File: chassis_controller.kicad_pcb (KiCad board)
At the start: 2 copper layers, 100 x 75 mm, 151 parts, among them J1 Screw_Terminal_01x02, J10 Conn_01x04_Pin, J12 Conn_01x04_Pin, J13 Conn_01x04_Pin, J14 Conn_01x04_Pin, J15 Conn_01x04_Pin, J16 Conn_01x04_Pin, J17 Conn_01x04_Pin, J18 Conn_01x03_Pin, J19 Conn_01x03_Pin, J2 Conn_01x04_Pin, J20 Conn_01x03_Pin, J21 Conn_01x04_Pin, J22 Conn_01x03_Pin, J23 Conn_01x03_Pin, J24 Conn_01x03_Pin, J25 Conn_01x03_Pin, J26 Conn_01x06_Pin, J3 Screw_Terminal_01x02, J4 Conn_01x02_Pin, J5 Conn_01x03_Pin, J6 Conn_01x03_Pin, J7 Conn_01x04_Pin, J8 Conn_01x04_Pin, J9 Conn_01x04_Pin, Q1 NMOS, Q2 HSBA100P04, Q3 NMOS, Q4 HSBA100P04, U1 AP64500SP-13, U2 AMS1117-3.3, U3 DSHP04TSGER, U4 STM32F407VGT6TR, U5 PCA9685PW,118, U6 PCA9685PW,118, U7 MPU-6050, U8 SN65HVD230DR, X1 X32258MOB4SI

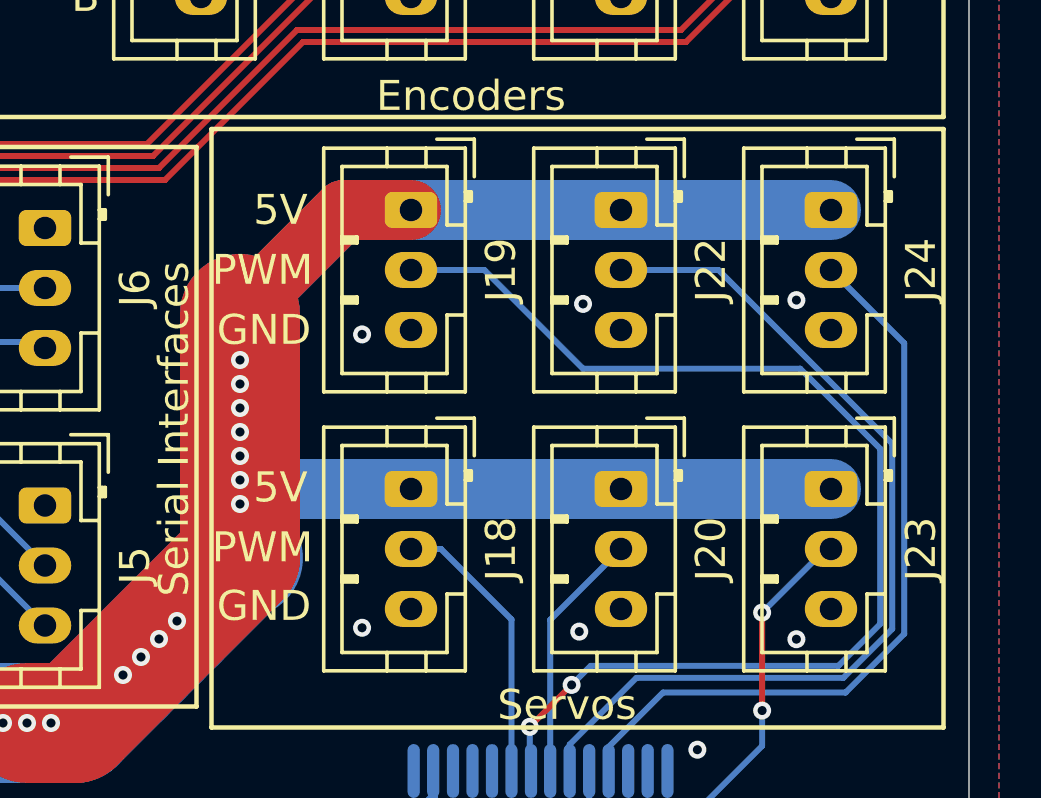
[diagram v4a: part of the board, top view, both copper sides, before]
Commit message: Fix servo power line
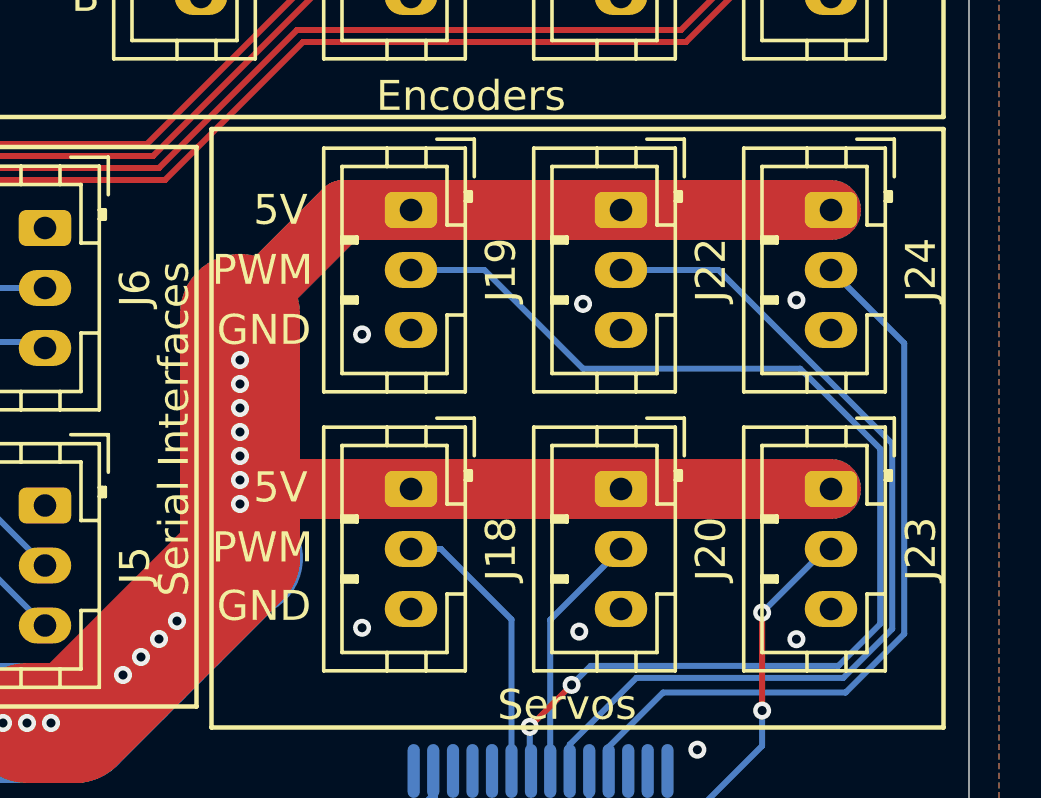
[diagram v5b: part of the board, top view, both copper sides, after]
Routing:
- net /SERVO_5V: track 95.4 -> 129.2 mm
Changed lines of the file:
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@@
+	)
+	(segment
+		(start 192.4 105.2)
+		(end 199.4 105.2)
+		(width 2)
+		(layer "F.Cu")
+		(net 63)
 	)
 	(segment
@@
 	)
 	(segment
+		(start 185.4 114.5)
+		(end 192.4 114.5)
+		(width 2)
+		(layer "F.Cu")
+		(net 63)
+	)
+	(segment
 		(start 179.7 110.2)
 		(end 179.7 108.663788)
@@
 	(segment
 		(start 179.7 116.786212)
-		(end 179.7 110.2)
-		(width 4)
+		(end 179.7 114.3)
+		(width 4)
+		(layer "F.Cu")
+		(net 63)
+	)
+	(segment
+		(start 185.4 105.2)
+		(end 192.4 105.2)
+		(width 2)
 		(layer "F.Cu")
 		(net 63)
@@
 	)
 	(segment
+		(start 192.4 114.5)
+		(end 199.4 114.5)
+		(width 2)
+		(layer "F.Cu")
+		(net 63)
+	)
+	(segment
+		(start 179.7 114.3)
+		(end 179.9 114.5)
+		(width 2)
+		(layer "F.Cu")
+		(net 63)
+	)
+	(segment
 		(start 174.186212 122.3)
 		(end 179.7 116.786212)
@@
 	)
 	(segment
+		(start 179.9 114.5)
+		(end 185.4 114.5)
+		(width 2)
+		(layer "F.Cu")
+		(net 63)
+	)
+	(segment
+		(start 179.7 114.3)
+		(end 179.7 110.2)
+		(width 4)
+		(layer "F.Cu")
+		(net 63)
+	)
+	(segment
 		(start 185.4 105.2)
 		(end 183.163788 105.2)
@@
 	)
 	(segment
+		(start 192.4 114.5)
+		(end 199.4 114.5)
+		(width 2)
+		(layer "B.Cu")
+		(net 63)
+	)
+	(segment
 		(start 179.7 111)
 		(end 179.7 110.2)
@@
 	)
 	(segment
+		(start 185.4 114.5)
+		(end 192.4 114.5)
+		(width 2)
+		(layer "B.Cu")
+		(net 63)
+	)
+	(segment
+		(start 180 114.5)
+		(end 179.7 114.2)
+		(width 2)
+		(layer "B.Cu")
+		(net 63)
+	)
+	(segment
+		(start 170.2 122.3)
+		(end 171 122.3)
+		(width 4)
+		(layer "B.Cu")
+		(net 63)
+	)
+	(segment
+		(start 171.8 122.3)
+		(end 172.6 122.3)
+		(width 4)
+		(layer "B.Cu")
+		(net 63)
+	)
+	(segment
+		(start 192.4 105.2)
+		(end 199.4 105.2)
+		(width 2)
+		(layer "B.Cu")
+		(net 63)
+	)
+	(segment
+		(start 177.6 118.9)
+		(end 179.7 116.8)
+		(width 4)
+		(layer "B.Cu")
+		(net 63)
+	)
+	(segment
+		(start 179.7 114.2)
+		(end 179.7 113.4)
+		(width 4)
+		(layer "B.Cu")
+		(net 63)
+	)
+	(segment
+		(start 179.7 116.8)
+		(end 179.7 115)
+		(width 4)
+		(layer "B.Cu")
+		(net 63)
+	)
+	(segment
+		(start 165.06 125.234336)
+		(end 167.994336 122.3)
+		(width 4)
+		(layer "B.Cu")
+		(net 63)
+	)
+	(segment
+		(start 167.994336 122.3)
+		(end 170.2 122.3)
+		(width 4)
+		(layer "B.Cu")
+		(net 63)
+	)
+	(segment
+		(start 179.7 116.8)
+		(end 179.8 116.8)
+		(width 4)
+		(layer "B.Cu")
+		(net 63)
+	)
+	(segment
+		(start 171 122.3)
+		(end 171.8 122.3)
+		(width 4)
+		(layer "B.Cu")
+		(net 63)
+	)
+	(segment
+		(start 176.4 120.1)
+		(end 177 119.5)
+		(width 4)
+		(layer "B.Cu")
+		(net 63)
+	)
+	(segment
+		(start 173.4 122.3)
+		(end 174.2 122.3)
+		(width 4)
+		(layer "B.Cu")
+		(net 63)
+	)
+	(segment
+		(start 165.06 128.645)
+		(end 165.06 125.234336)
+		(width 4)
+		(layer "B.Cu")
+		(net 63)
+	)
+	(segment
+		(start 179.7 111.8)
+		(end 179.7 111)
+		(width 4)
+		(layer "B.Cu")
+		(net 63)
+	)
+	(segment
+		(start 175.8 120.7)
+		(end 176.4 120.1)
+		(width 4)
+		(layer "B.Cu")
+		(net 63)
+	)
+	(segment
+		(start 179.7 110.2)
+		(end 179.7 108.663788)
+		(width 4)
+		(layer "B.Cu")
+		(net 63)
+	)
+	(segment
+		(start 179.7 108.663788)
+		(end 183.163788 105.2)
+		(width 2)
+		(layer "B.Cu")
+		(net 63)
+	)
+	(segment
 		(start 185.4 105.2)
 		(end 192.4 105.2)
 		(width 2)
 		(layer "B.Cu")
-		(net 63)
-	)
-	(segment
-		(start 180 114.5)
-		(end 179.7 114.2)
-		(width 2)
-		(layer "B.Cu")
-		(net 63)
-	)
-	(segment
-		(start 170.2 122.3)
-		(end 171 122.3)
-		(width 4)
-		(layer "B.Cu")
-		(net 63)
-	)
-	(segment
-		(start 171.8 122.3)
-		(end 172.6 122.3)
-		(width 4)
-		(layer "B.Cu")
-		(net 63)
-	)
-	(segment
-		(start 177.6 118.9)
-		(end 179.7 116.8)
-		(width 4)
-		(layer "B.Cu")
-		(net 63)
-	)
-	(segment
-		(start 199.4 114.5)
-		(end 192.4 114.5)
-		(width 2)
-		(layer "B.Cu")
-		(net 63)
-	)
-	(segment
-		(start 179.7 114.2)
-		(end 179.7 113.4)
-		(width 4)
-		(layer "B.Cu")
-		(net 63)
-	)
-	(segment
-		(start 192.4 105.2)
-		(end 199.4 105.2)
-		(width 2)
-		(layer "B.Cu")
-		(net 63)
-	)
-	(segment
-		(start 179.7 116.8)
-		(end 179.7 115)
-		(width 4)
-		(layer "B.Cu")
-		(net 63)
-	)
-	(segment
-		(start 165.06 125.234336)
-		(end 167.994336 122.3)
-		(width 4)
-		(layer "B.Cu")
-		(net 63)
-	)
-	(segment
-		(start 167.994336 122.3)
-		(end 170.2 122.3)
-		(width 4)
-		(layer "B.Cu")
-		(net 63)
-	)
-	(segment
-		(start 179.7 116.8)
-		(end 179.8 116.8)
-		(width 4)
-		(layer "B.Cu")
-		(net 63)
-	)
-	(segment
-		(start 171 122.3)
-		(end 171.8 122.3)
-		(width 4)
-		(layer "B.Cu")
-		(net 63)
-	)
-	(segment
-		(start 176.4 120.1)
-		(end 177 119.5)
-		(width 4)
-		(layer "B.Cu")
-		(net 63)
-	)
-	(segment
-		(start 173.4 122.3)
-		(end 174.2 122.3)
-		(width 4)
-		(layer "B.Cu")
-		(net 63)
-	)
-	(segment
-		(start 192.4 114.5)
-		(end 185.4 114.5)
-		(width 2)
-		(layer "B.Cu")
-		(net 63)
-	)
-	(segment
-		(start 165.06 128.645)
-		(end 165.06 125.234336)
-		(width 4)
-		(layer "B.Cu")
-		(net 63)
-	)
-	(segment
-		(start 179.7 111.8)
-		(end 179.7 111)
-		(width 4)
-		(layer "B.Cu")
-		(net 63)
-	)
-	(segment
-		(start 175.8 120.7)
-		(end 176.4 120.1)
-		(width 4)
-		(layer "B.Cu")
-		(net 63)
-	)
-	(segment
-		(start 179.7 110.2)
-		(end 179.7 108.663788)
-		(width 4)
-		(layer "B.Cu")
-		(net 63)
-	)
-	(segment
-		(start 179.7 108.663788)
-		(end 183.163788 105.2)
-		(width 2)
-		(layer "B.Cu")
